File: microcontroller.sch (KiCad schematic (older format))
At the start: 48 parts, among them P1 Debug, P2 SPI1, P4 CONN_02X05, P5 CONN_02X05, Q2 SFH3711, SW1 SW_PUSH, SW2 SW_PUSH, SW3 SW_PUSH, U2 SN74LVC1G08, U3 STM32F072RB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

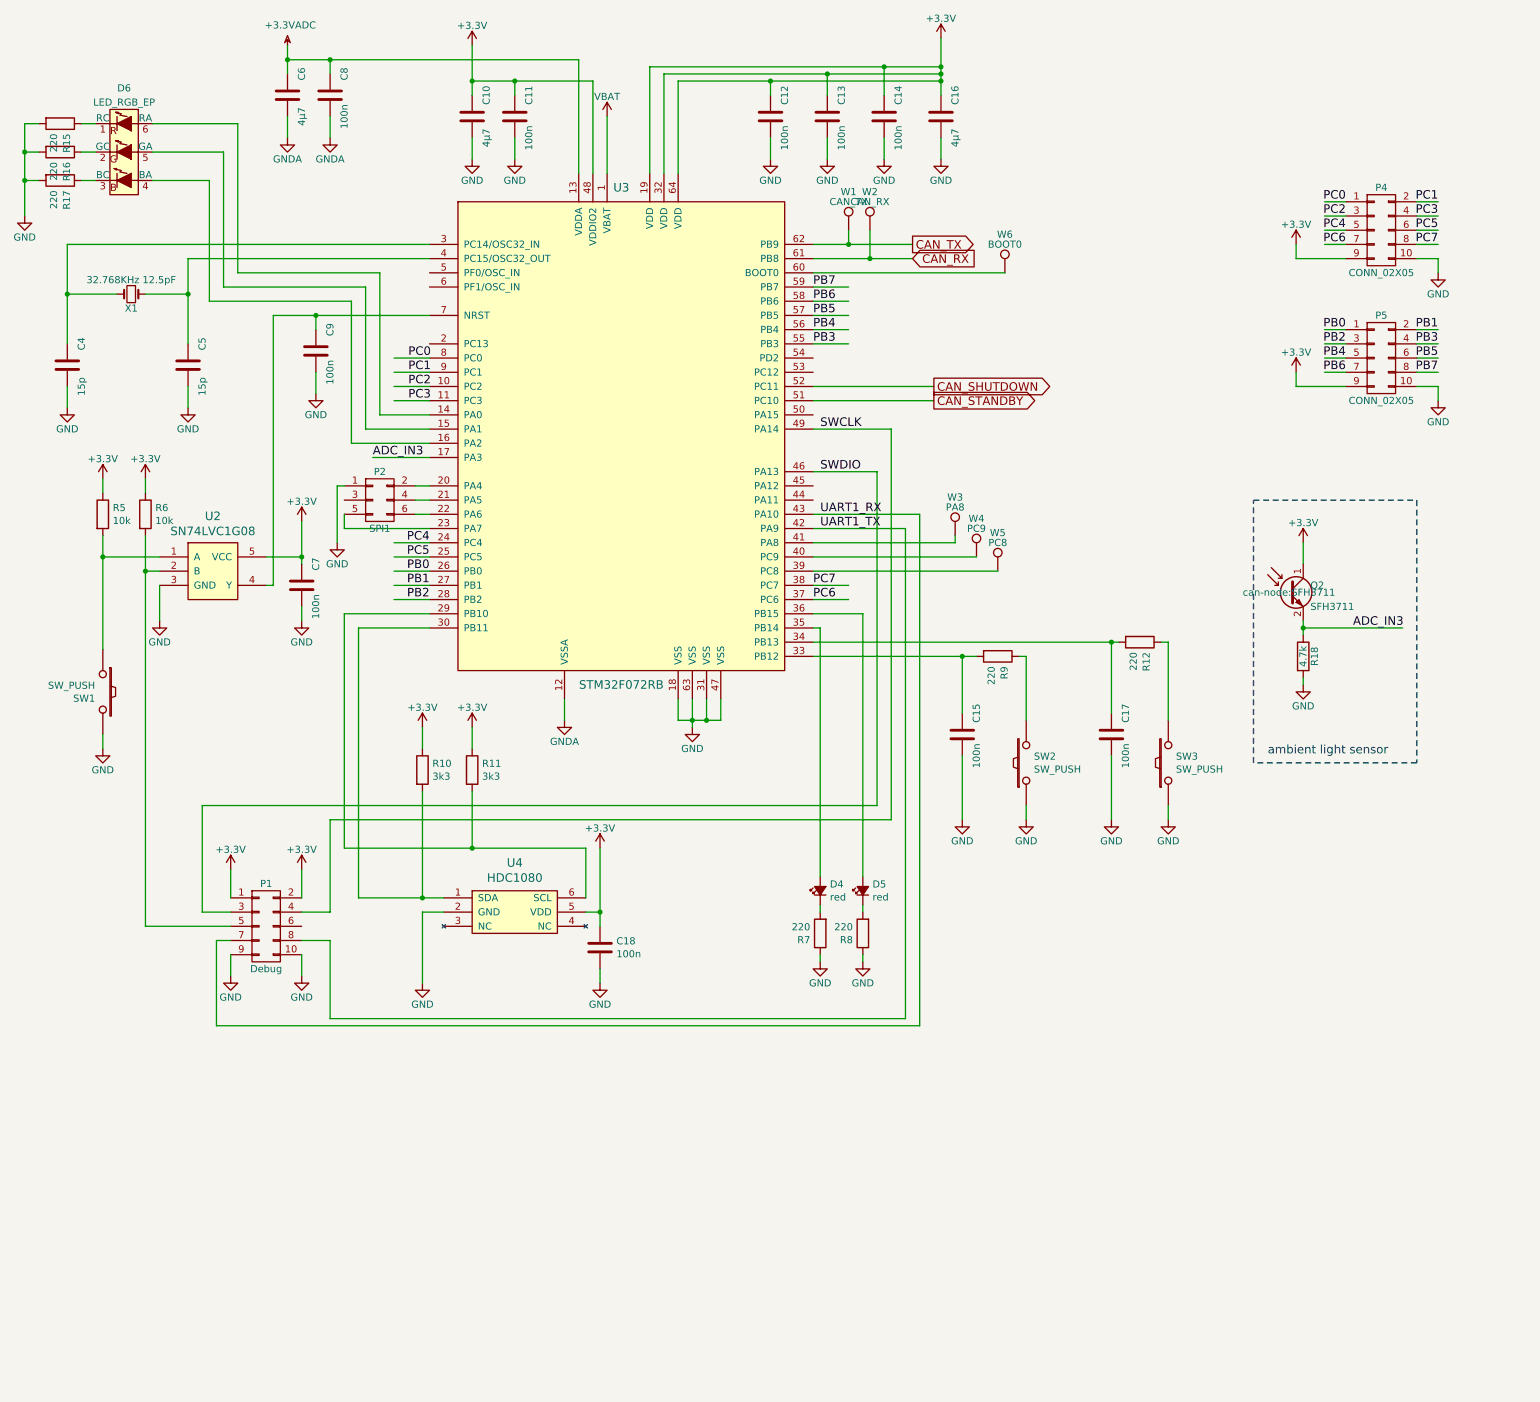
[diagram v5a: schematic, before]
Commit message: Some modifications to schematic, BOM, start releayout
- add LED display
- change crystal for RTC
- use components that are available at some distributors
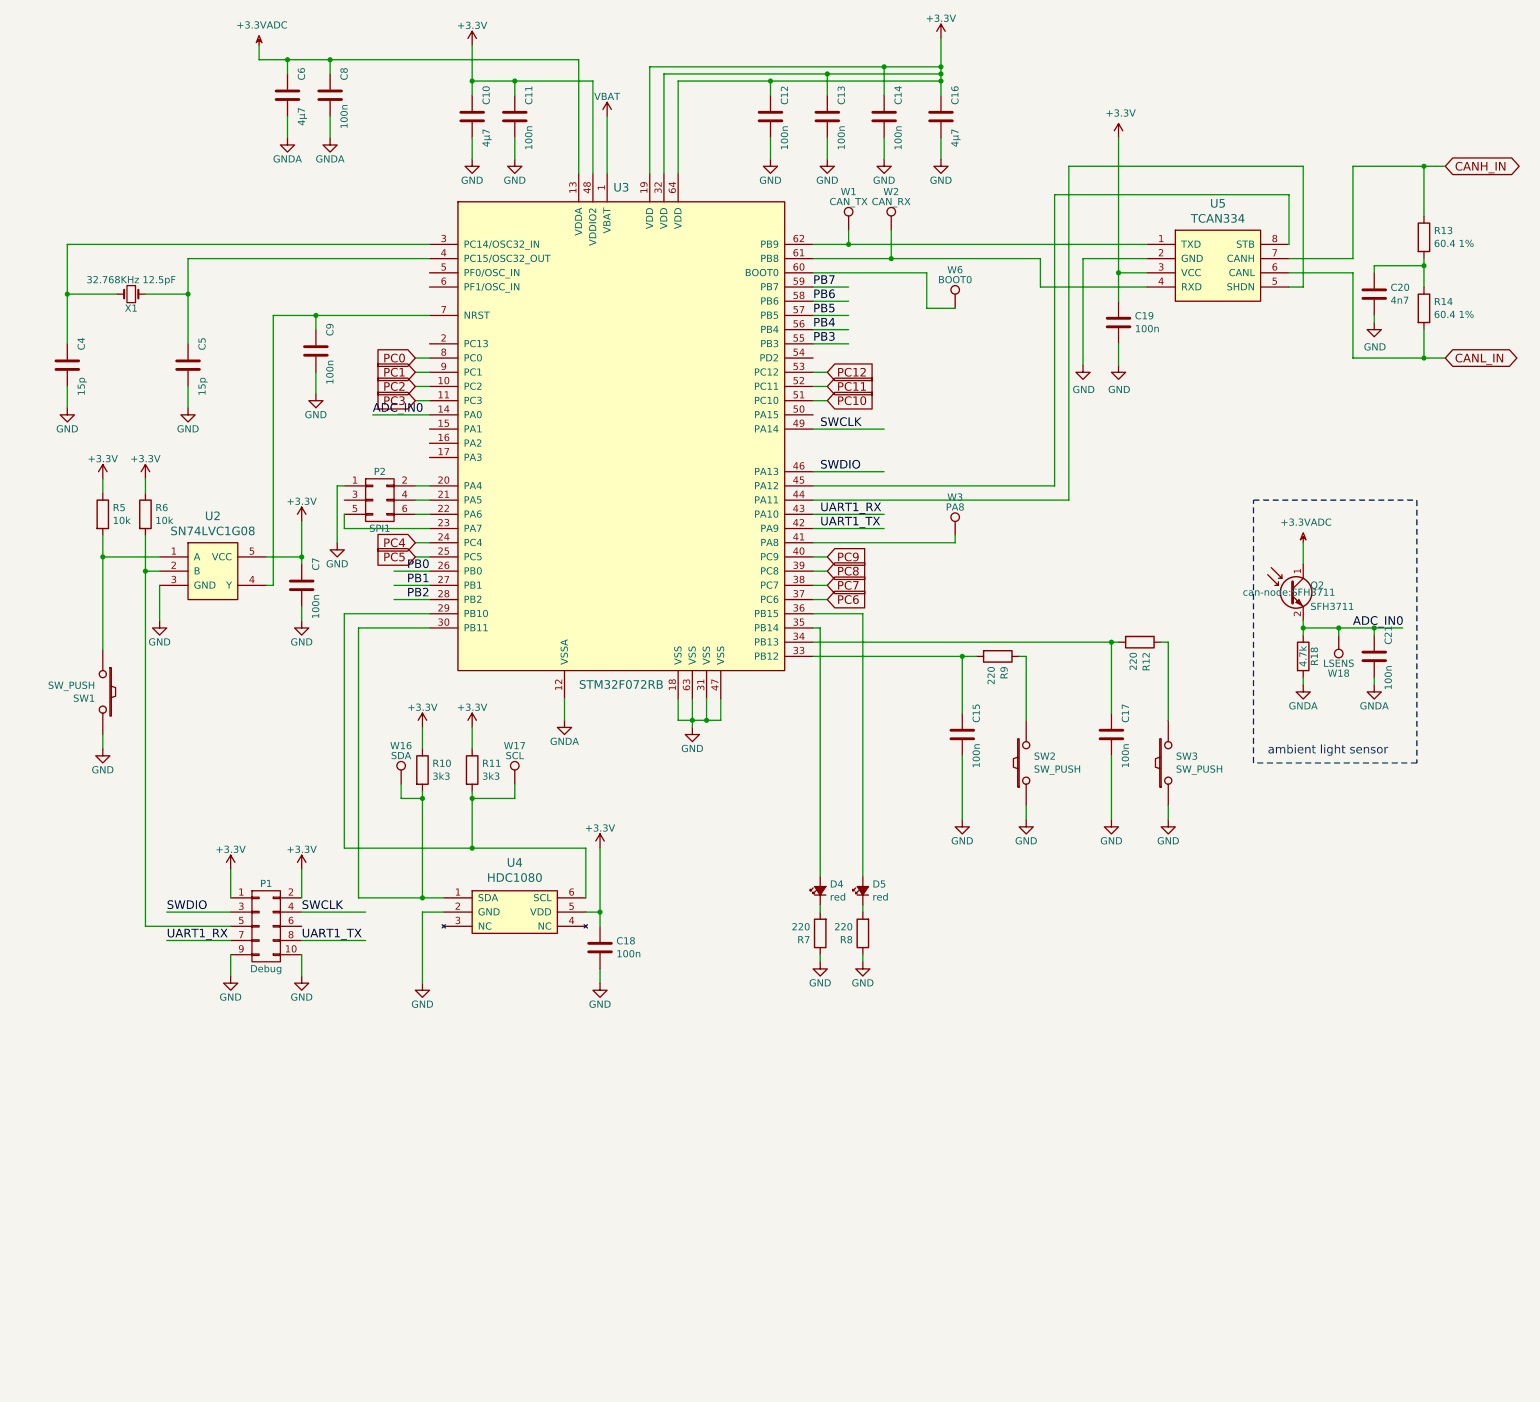
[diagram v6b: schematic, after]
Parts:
- removed D6: LED_RGB_EP, CAN_Node:Everlight_19-337, symbol LED_RGB_6P
- removed P4, P5: CONN_02X05, CAN_Node:PIN_Header_SMD_2.54mm_02x05, symbol CONN_02X05
- removed R15, R16, R17: 220, Resistors_SMD:R_0402, symbol R
- removed W4: PC9, can-node:Measurement_Point_tiny, symbol TEST_1P
- removed W5: PC8, can-node:Measurement_Point_tiny, symbol TEST_1P
- added C19, C21: 100n, Capacitors_SMD:C_0603, symbol C
- added C20: 4n7, Capacitors_SMD:C_0603, symbol C
- added R13, R14: 60.4 1%, Resistors_SMD:R_0402, symbol R
- added U5: TCAN334, can-node:TI-DCN, symbol TCAN334
- added W16: SDA, can-node:Measurement_Point_tiny, symbol TEST_1P
- added W17: SCL, can-node:Measurement_Point_tiny, symbol TEST_1P
- added W18: LSENS, can-node:Measurement_Point_tiny, symbol TEST_1P
- C11, C12, C13, C14, C15, C17, C18, C4, C5, C7, C8, C9: footprint Capacitors_SMD:C_0402 -> Capacitors_SMD:C_0603
- P1: footprint CAN_Node:micromatch_smd_2x05 -> can-node:micromatch_smd_2x05
- SW1, SW2, SW3: footprint CAN_Node:KMR2 -> can-node:KMR2
- U2: footprint CAN_Node:TI-DCK -> can-node:TI-DCK
- U4: footprint CAN_Node:HDC1080 -> can-node:HDC1080
- X1: footprint CAN_Node:Crystal_DT-26 -> can-node:Crystal-MS1V-T1K
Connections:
- net labels added: ADC_IN0, CANH_IN, CANL_IN, PC10, PC11, PC12, PC8, PC9
- net labels removed: ADC_IN3, CAN_RX, CAN_SHUTDOWN, CAN_STANDBY, CAN_TX
- wire segments 203 -> 184
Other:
- moved on the sheet: W2, W6

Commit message: Layouting work
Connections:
- net labels added: PA1, PA2
- wire segments 184 -> 182
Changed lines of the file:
@@
 Connection ~ 10500 2350
 Wire Wire Line
-	9550 1850 9550 2200
+	9550 1750 9550 2200
 Wire Wire Line
-	7900 1850 9550 1850
+	7850 1750 9550 1750
 $Comp
 L C C19
@@
 $EndComp
 Wire Wire Line
-	8000 1650 9650 1650
+	7850 1650 9650 1650
 Wire Wire Line
 	9650 1650 9650 2500
@@
 Wire Wire Line
 	7000 2650 7200 2650
-Wire Wire Line
-	8000 1650 8000 4000
-Wire Wire Line
-	7900 1850 7900 3900
 Wire Wire Line
 	6200 4100 6700 4100
@@
 	6200 4500 6300 4500
 Wire Wire Line
-	8000 4000 6200 4000
-Wire Wire Line
-	7900 3900 6200 3900
-Wire Wire Line
 	6200 3100 6300 3100
 Wire Wire Line
@@
 	1    0    0    -1
 $EndComp
+Text Label 3500 3500 2    60   ~ 0
+PA1
+Text Label 3500 3600 2    60   ~ 0
+PA2
+Wire Wire Line
+	3350 3500 3500 3500
+Wire Wire Line
+	3350 3600 3500 3600
+Text Label 8000 1650 2    60   ~ 0
+PA1
+Text Label 8000 1750 2    60   ~ 0
+PA2
 $EndSCHEMATC

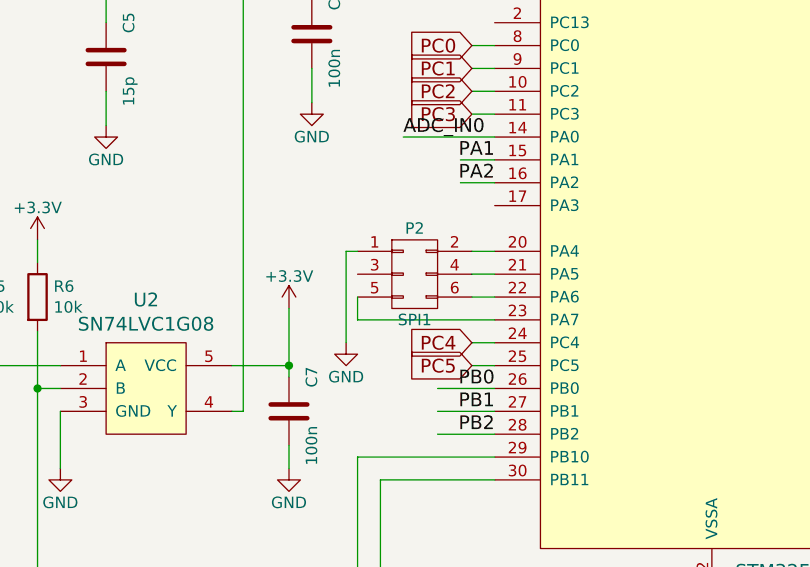
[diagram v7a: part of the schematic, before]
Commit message: Remove spi connector.
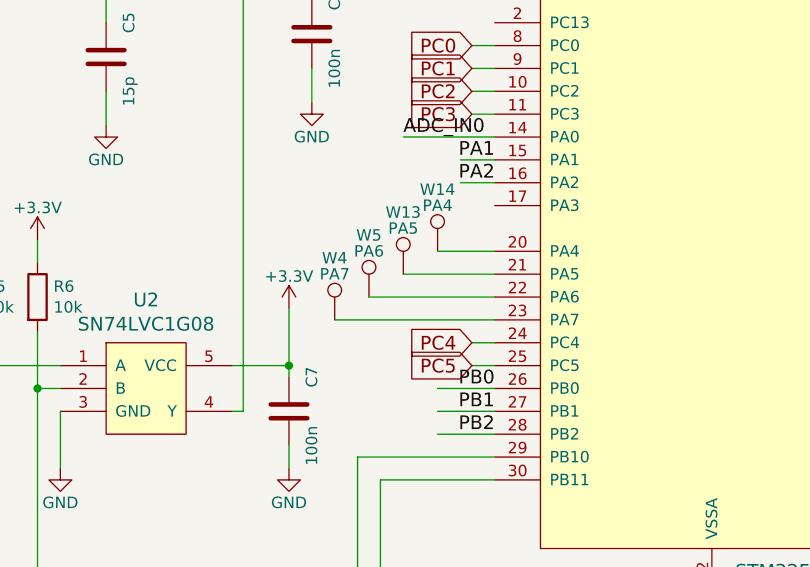
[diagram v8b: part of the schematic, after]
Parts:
- removed P2: SPI1, can-node:PIN_Header_SMD_2.54mm_02x03, symbol CONN_02X03
- added W13: PA5, can-node:Measurement_Point_tiny, symbol TEST_1P
- added W14: PA4, can-node:Measurement_Point_tiny, symbol TEST_1P
- added W4: PA7, can-node:Measurement_Point_tiny, symbol TEST_1P
- added W5: PA6, can-node:Measurement_Point_tiny, symbol TEST_1P
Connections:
- wire segments 182 -> 179
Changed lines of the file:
@@
-	1    0    0    -1
-$EndComp
-$Comp
-L GND #PWR054
-U 1 1 58441195
-P 2850 4300
-F 0 "#PWR054" H 2850 4050 50  0001 C CNN
-F 1 "GND" H 2850 4150 50  0000 C CNN
-F 2 "" H 2850 4300 60  0000 C CNN
-F 3 "" H 2850 4300 60  0000 C CNN
-	1    2850 4300
-	1    0    0    -1
-$EndComp
-$Comp
-L CONN_02X03 P2
-U 1 1 584408D4
-P 3150 4000
-F 0 "P2" H 3150 4200 50  0000 C CNN
-F 1 "SPI1" H 3150 3800 50  0000 C CNN
-F 2 "can-node:PIN_Header_SMD_2.54mm_02x03" H 3150 2800 50  0001 C CNN
-F 3 "" H 3150 2800 50  0000 C CNN
-	1    3150 4000
 	1    0    0    -1
 $EndComp
@@
 	1650 7100 2100 7100
 Wire Wire Line
-	3500 4000 3400 4000
-Wire Wire Line
-	3500 3900 3400 3900
-Wire Wire Line
-	3500 4100 3400 4100
-Wire Wire Line
-	3500 4200 2900 4200
-Wire Wire Line
-	2900 4200 2900 4100
-Wire Wire Line
-	2850 4300 2850 3900
-Wire Wire Line
-	2850 3900 2900 3900
+	3500 4000 3100 4000
+Wire Wire Line
+	3500 3900 3250 3900
+Wire Wire Line
+	3500 4100 2950 4100
+Wire Wire Line
+	2800 4200 3500 4200
 $Comp
 L TEST_1P W3
@@
 	7800 2500 8550 2500
 $Comp
-L GND #PWR055
+L GND #PWR054
 U 1 1 586A5CF0
 P 8100 3050
-F 0 "#PWR055" H 8100 2800 50  0001 C CNN
+F 0 "#PWR054" H 8100 2800 50  0001 C CNN
 F 1 "GND" H 8105 2877 50  0000 C CNN
 F 2 "" H 8100 3050 50  0000 C CNN
@@
 	8350 1450 8350 2600
 $Comp
-L +3.3V #PWR056
+L +3.3V #PWR055
 U 1 1 586A5CFA
 P 8350 1450
-F 0 "#PWR056" H 8350 1300 50  0001 C CNN
+F 0 "#PWR055" H 8350 1300 50  0001 C CNN
 F 1 "+3.3V" H 8365 1623 50  0000 C CNN
 F 2 "" H 8350 1450 50  0000 C CNN
@@
 $EndComp
 $Comp
-L GND #PWR057
+L GND #PWR056
 U 1 1 586A5D22
 P 10150 2750
-F 0 "#PWR057" H 10150 2500 50  0001 C CNN
+F 0 "#PWR056" H 10150 2500 50  0001 C CNN
 F 1 "GND" H 10155 2577 50  0000 C CNN
 F 2 "" H 10150 2750 50  0000 C CNN
@@
 $EndComp
 $Comp
-L GND #PWR058
+L GND #PWR057
 U 1 1 586A5D36
 P 8350 3050
-F 0 "#PWR058" H 8350 2800 50  0001 C CNN
+F 0 "#PWR057" H 8350 2800 50  0001 C CNN
 F 1 "GND" H 8355 2877 50  0000 C CNN
 F 2 "" H 8350 3050 50  0000 C CNN
@@
 	2300 900  2300 800
 $Comp
-L GNDA #PWR059
+L GNDA #PWR058
 U 1 1 586DE8F0
 P 9650 5300
-F 0 "#PWR059" H 9650 5050 50  0001 C CNN
+F 0 "#PWR058" H 9650 5050 50  0001 C CNN
 F 1 "GNDA" H 9650 5150 50  0000 C CNN
 F 2 "" H 9650 5300 60  0000 C CNN
@@
 $EndComp
 $Comp
-L GNDA #PWR060
+L GNDA #PWR059
 U 1 1 586DEB22
 P 10150 5300
-F 0 "#PWR060" H 10150 5050 50  0001 C CNN
+F 0 "#PWR059" H 10150 5050 50  0001 C CNN
 F 1 "GNDA" H 10150 5150 50  0000 C CNN
 F 2 "" H 10150 5300 60  0000 C CNN
@@
 $EndComp
 $Comp
-L +3.3VADC #PWR061
+L +3.3VADC #PWR060
 U 1 1 586DF2A5
 P 9650 4300
-F 0 "#PWR061" H 9800 4250 50  0001 C CNN
+F 0 "#PWR060" H 9800 4250 50  0001 C CNN
 F 1 "+3.3VADC" H 9670 4443 50  0000 C CNN
 F 2 "" H 9650 4300 50  0000 C CNN
@@
 Text Label 8000 1750 2    60   ~ 0
 PA2
+$Comp
+L TEST_1P W14
+U 1 1 5870BC17
+P 3250 3900
+F 0 "W14" H 3250 4170 50  0000 C CNN
+F 1 "PA4" H 3250 4100 50  0000 C CNN
+F 2 "can-node:Measurement_Point_tiny" H 3450 3900 50  0001 C CNN
+F 3 "" H 3450 3900 50  0000 C CNN
+	1    3250 3900
+	1    0    0    -1
+$EndComp
+$Comp
+L TEST_1P W13
+U 1 1 5870C01C
+P 3100 4000
+F 0 "W13" H 3100 4270 50  0000 C CNN
+F 1 "PA5" H 3100 4200 50  0000 C CNN
+F 2 "can-node:Measurement_Point_tiny" H 3300 4000 50  0001 C CNN
+F 3 "" H 3300 4000 50  0000 C CNN
+	1    3100 4000
+	1    0    0    -1
+$EndComp
+$Comp
+L TEST_1P W5
+U 1 1 5870C0CE
+P 2950 4100
+F 0 "W5" H 2950 4370 50  0000 C CNN
+F 1 "PA6" H 2950 4300 50  0000 C CNN
+F 2 "can-node:Measurement_Point_tiny" H 3150 4100 50  0001 C CNN
+F 3 "" H 3150 4100 50  0000 C CNN
+	1    2950 4100
+	1    0    0    -1
+$EndComp
+$Comp
+L TEST_1P W4
+U 1 1 5870C17F
+P 2800 4200
+F 0 "W4" H 2800 4470 50  0000 C CNN
+F 1 "PA7" H 2800 4400 50  0000 C CNN
+F 2 "can-node:Measurement_Point_tiny" H 3000 4200 50  0001 C CNN
+F 3 "" H 3000 4200 50  0000 C CNN
+	1    2800 4200
+	1    0    0    -1
+$EndComp
 $EndSCHEMATC
